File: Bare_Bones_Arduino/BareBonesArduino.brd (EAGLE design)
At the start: 43.2 x 61 mm, 15 parts, among them U1 ATMEGA328P_PDIP

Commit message: Version 2 smaller design
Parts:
- removed JP3: AVR_SPI_PRG_6PTH, SparkFun-Connectors:2X3
- added JP5: (no value), SparkFun-Connectors:1X06
- moved D3 31.0 mm to (15.2, 44.5), turned to 180 degrees
- moved R1 30.5 mm to (10.4, 45.7), turned to 90 degrees
- moved R3 27.2 mm to (19.1, 38.1), turned to 179.3 degrees
- moved D1 25.7 mm to (15.2, 50.8), turned to 180 degrees
- moved R2 21.9 mm to (19.1, 35.6), turned to 0 degrees
- moved JP2 11.7 mm to (34.0, 59.7)
- moved D2 11.4 mm to (29.2, 36.8), turned to 270 degrees
- moved JP4 8.65 mm to (5.59, 55.6)
- moved C1 4.02 mm to (15.2, 59.7)
- moved U1 2.84 mm to (24.1, 58.4)
- moved R4 1.77 mm to (10.8, 66.4)
- moved C2 0.52 mm to (5.59, 59.6), turned to 90 degrees
- moved JP1 0.25 mm to (1.52, 74.9)
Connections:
- net GND: now also JP5.1; no longer JP3.6
- net MISO: now also JP5.3; no longer JP3.1
- net MOSI: now also JP5.2; no longer JP3.4
- net RESET: now also JP5.6; no longer JP3.5
- net SCK: now also JP5.4; no longer JP3.3
- net VCC: now also JP5.5; no longer JP3.2
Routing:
- net GND: track 152.0 -> 0.00 mm
- net VCC: track 94.9 -> 63.7 mm
- net MISO: track 34.3 -> 6.62 mm, vias 1 -> 0
- net N$5: track 32.3 -> 4.86 mm
- net RESET: track 74.0 -> 51.1 mm
- net SCK: track 27.2 -> 6.62 mm
- net N$13: track 15.9 -> 6.10 mm
- net N$12: track 15.9 -> 6.10 mm
- net N$11: track 15.8 -> 6.10 mm
- net N$10: track 15.8 -> 6.10 mm
- net N$9: track 15.8 -> 6.10 mm
- net N$8: track 15.8 -> 6.10 mm
- net DTR: track 12.7 -> 3.94 mm
- net RX: track 37.3 -> 28.7 mm, vias 1 -> 0
- net TX: track 31.4 -> 23.2 mm
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- added copper zone on layer 16, net GND
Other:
- board size 43.2 x 61 mm -> 31.8 x 45.7 mm
- board text added: "C1"
- board text added: "C2"
- board text added: "MIS"
- board text added: "MOS"
- board text added: "R1"
- board text added: "R2"
- board text added: "R3"
- board text added: "R4"
- board text added: "RST"
- board text added: "SCK"
- board text removed: "0.1uF"
- board text removed: "1K"
- board text removed: "330"
- board text removed: "Arduino - 1st PCB"
- board text removed: "Bare Bones"
- board text removed: "DTR"
- board text removed: "JG"
- board text removed: "TX RX VCC CTS GND"

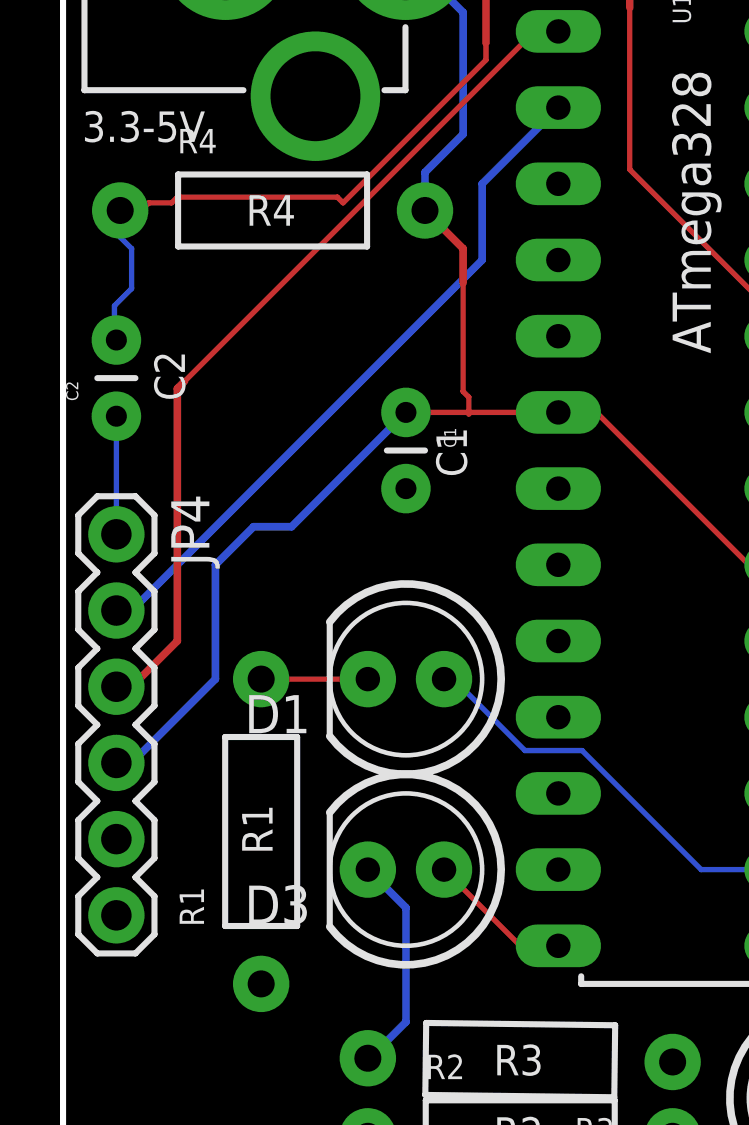
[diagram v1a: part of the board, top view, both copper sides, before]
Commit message: Version 2.  Forgot Silks, fix TX/RX
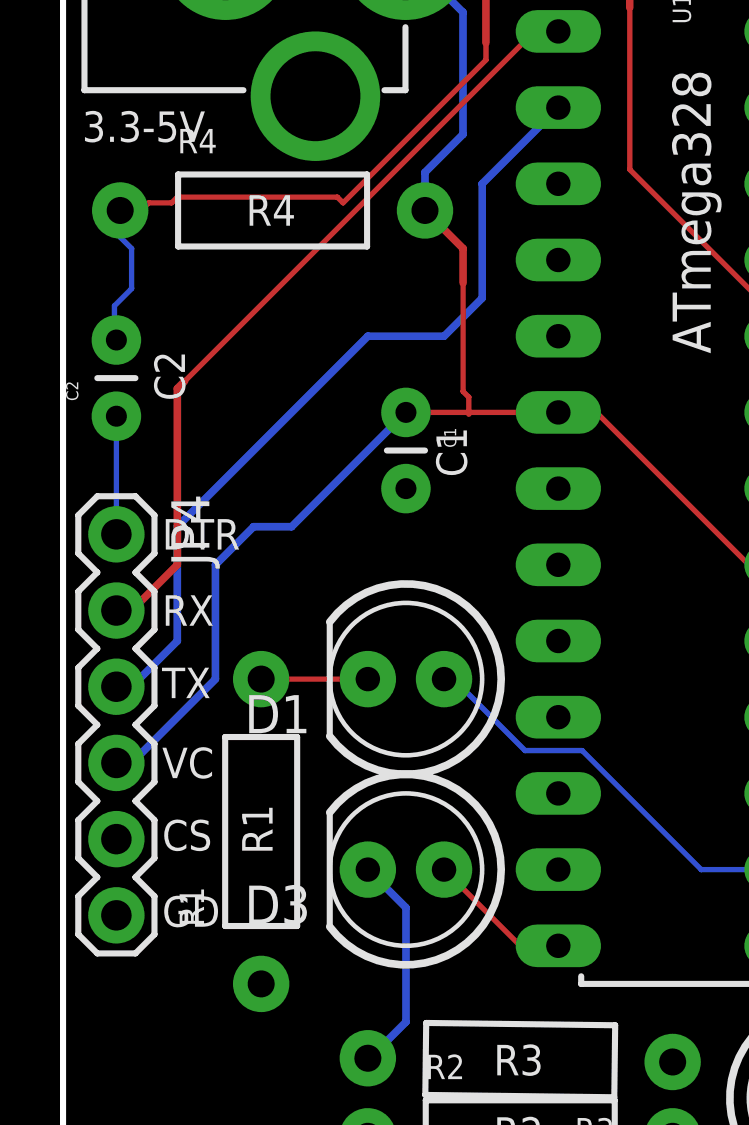
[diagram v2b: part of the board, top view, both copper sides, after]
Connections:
- net RX: now also JP4.2; no longer JP4.3
- net TX: now also JP4.3; no longer JP4.2
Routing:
- net TX: track 23.2 -> 27.2 mm
- net RX: track 28.7 -> 26.2 mm
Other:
- board text added: "CS"
- board text added: "DTR"
- board text added: "GD"
- board text added: "RX"
- board text added: "TX"
- board text added: "VC"
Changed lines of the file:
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@@
 <dimension x1="-1.27" y1="80.01" x2="0" y2="34.29" x3="0" y3="57.15" textsize="1.778" layer="20" dtype="vertical" unit="inch"/>
 <dimension x1="35.56" y1="29.21" x2="3.81" y2="30.48" x3="19.685" y3="30.48" textsize="1.778" layer="20" dtype="horizontal" unit="inch"/>
+<text x="7.112" y="55.118" size="1.016" layer="21" font="vector" ratio="15">DTR</text>
+<text x="7.112" y="52.578" size="1.016" layer="21" font="vector" ratio="15">RX</text>
+<text x="7.112" y="50.165" size="1.016" layer="21" font="vector" ratio="15">TX</text>
+<text x="7.112" y="47.498" size="1.016" layer="21" font="vector" ratio="15">VC</text>
+<text x="7.112" y="45.085" size="1.016" layer="21" font="vector" ratio="15">CS</text>
+<text x="7.112" y="42.545" size="1.016" layer="21" font="vector" ratio="15">GD</text>
 </plain>
 <attributes>
@@
 </signal>
 <signal name="RX">
-<contactref element="JP4" pad="3"/>
 <contactref element="U1" pad="2"/>
 <wire x1="19.52625" y1="72.39" x2="20.32" y2="72.39" width="0.1778" layer="1"/>
 <wire x1="7.858125" y1="60.721875" x2="19.52625" y2="72.39" width="0.1778" layer="1"/>
-<wire x1="5.588" y1="50.546" x2="6.096" y2="50.546" width="0.254" layer="1"/>
-<wire x1="6.096" y1="50.546" x2="7.62" y2="52.07" width="0.254" layer="1"/>
-<wire x1="7.62" y1="52.07" x2="7.62" y2="60.48375" width="0.254" layer="1"/>
 <wire x1="7.62" y1="60.48375" x2="7.858125" y2="60.721875" width="0.254" layer="1"/>
+<contactref element="JP4" pad="2"/>
+<wire x1="5.588" y1="53.086" x2="6.096" y2="53.086" width="0.254" layer="1"/>
+<wire x1="6.096" y1="53.086" x2="7.62" y2="54.61" width="0.254" layer="1"/>
+<wire x1="7.62" y1="54.61" x2="7.62" y2="60.48375" width="0.254" layer="1"/>
 </signal>
 <signal name="TX">
-<contactref element="JP4" pad="2"/>
 <contactref element="U1" pad="3"/>
-<wire x1="5.588" y1="53.086" x2="6.096" y2="53.086" width="0.254" layer="16"/>
-<wire x1="6.096" y1="53.086" x2="17.78" y2="64.77" width="0.254" layer="16"/>
-<wire x1="17.78" y1="64.77" x2="17.78" y2="67.31" width="0.254" layer="16"/>
+<contactref element="JP4" pad="3"/>
+<wire x1="5.588" y1="50.546" x2="6.096" y2="50.546" width="0.254" layer="16"/>
+<wire x1="6.096" y1="50.546" x2="7.62" y2="52.07" width="0.254" layer="16"/>
+<wire x1="7.62" y1="52.07" x2="7.62" y2="55.88" width="0.254" layer="16"/>
+<wire x1="7.62" y1="55.88" x2="13.97" y2="62.23" width="0.254" layer="16"/>
+<wire x1="13.97" y1="62.23" x2="16.51" y2="62.23" width="0.254" layer="16"/>
+<wire x1="16.51" y1="62.23" x2="17.78" y2="63.5" width="0.254" layer="16"/>
+<wire x1="17.78" y1="63.5" x2="17.78" y2="67.31" width="0.254" layer="16"/>
 <wire x1="17.78" y1="67.31" x2="20.32" y2="69.85" width="0.254" layer="16"/>
 </signal>
